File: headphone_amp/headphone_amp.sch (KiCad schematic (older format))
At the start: 16 parts, among them J1 Molex_SL_01x03_Male, J2 Molex_SL_01x02_Male

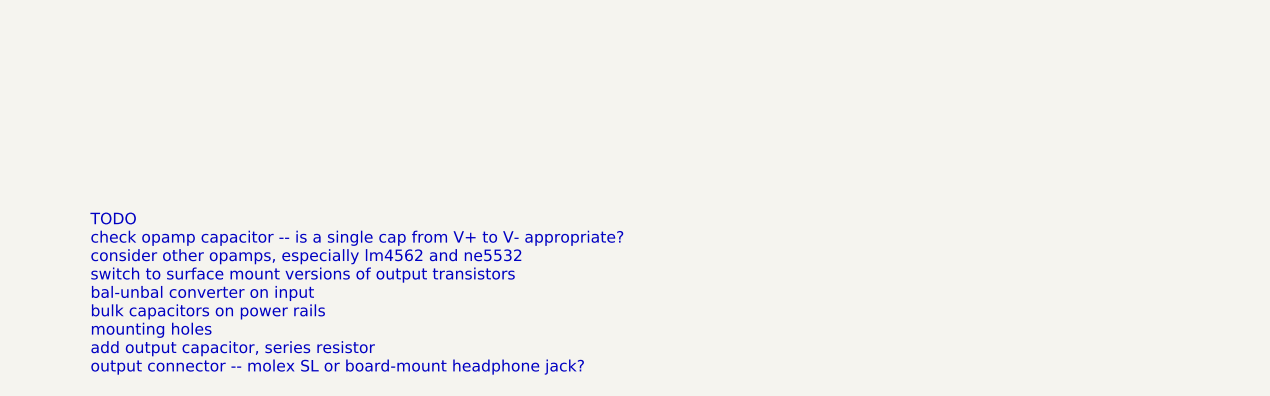
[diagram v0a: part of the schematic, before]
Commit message: update TODO and add license comment
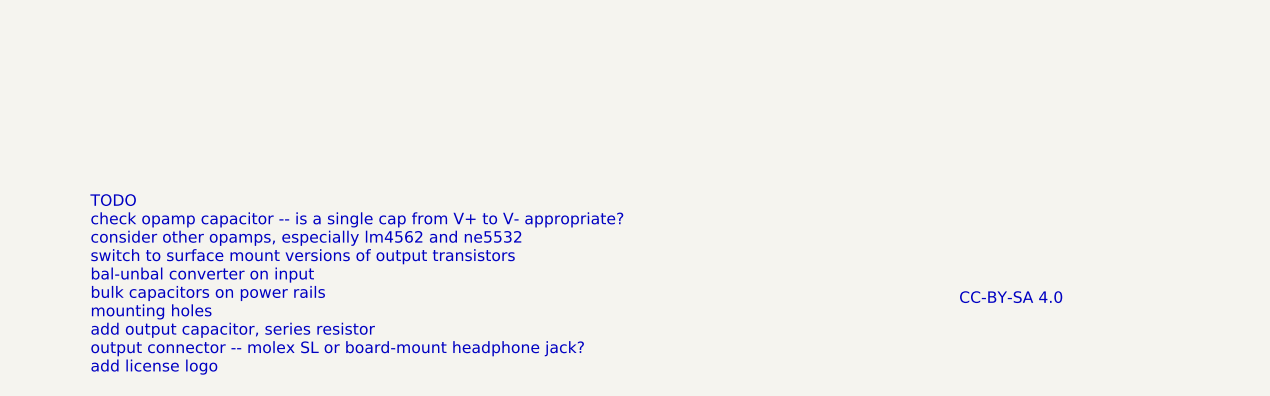
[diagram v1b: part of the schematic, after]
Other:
- note added: "CC-BY-SA 4.0"
- note added: "TODO\ncheck opamp capacitor -- is a single cap from V+ to V- appropriate?\nconsider other opamps, especially lm4562 and ne5532\nswitch to surface mount versions of output transistors\nbal-unbal converter on input\nbulk capacitors on power rails\nmounting holes\nadd output capacitor, series resistor\noutput connector -- molex SL or board-mount headphone jack?\nadd license logo"
- note removed: "TODO\ncheck opamp capacitor -- is a single cap from V+ to V- appropriate?\nconsider other opamps, especially lm4562 and ne5532\nswitch to surface mount versions of output transistors\nbal-unbal converter on input\nbulk capacitors on power rails\nmounting holes\nadd output capacitor, series resistor\noutput connector -- molex SL or board-mount headphone jack?"
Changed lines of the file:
@@
 Connection ~ 2150 1150
 Text Notes 1300 7550 0    50   ~ 0
-TODO\ncheck opamp capacitor -- is a single cap from V+ to V- appropriate?\nconsider other opamps, especially lm4562 and ne5532\nswitch to surface mount versions of output transistors\nbal-unbal converter on input\nbulk capacitors on power rails\nmounting holes\nadd output capacitor, series resistor\noutput connector -- molex SL or board-mount headphone jack?
+TODO\ncheck opamp capacitor -- is a single cap from V+ to V- appropriate?\nconsider other opamps, especially lm4562 and ne5532\nswitch to surface mount versions of output transistors\nbal-unbal converter on input\nbulk capacitors on power rails\nmounting holes\nadd output capacitor, series resistor\noutput connector -- molex SL or board-mount headphone jack?\nadd license logo
 $Comp
 L Connector_gkeeth:Molex_SL_01x02_Male J2
@@
 Text Label 2450 3150 0    50   ~ 0
 cold
+Text Notes 5100 7250 0    50   ~ 0
+CC-BY-SA 4.0
 $EndSCHEMATC

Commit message: Complete initial schematic for headphone amplifier
Features present:
- left and right channels
- input connectors, output jack
- balanced-to-unbalanced converters
- power connector
- bulk capacitance
- mounting holes

Remaining TODO:
- relay
- footprints
- surface mount output transistors
- output jack grounding?
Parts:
- removed R?: 10k, symbol Device:R
- removed U? (x3): TL072, symbol Amplifier_Operational:TL072
- added C1, C2, C4, C5: 22p, symbol Device:C
- added C3, C6, C8, C9: 220u, symbol Device:CP1
- added D3, D4: 1N4148WS, Diode_SMD:D_SOD-323, symbol Diode:1N4148WS
- added H1, H2: MountingHole_Pad, MountingHole:MountingHole_4.5mm_Pad, symbol Mechanical:MountingHole_Pad
- added J2: Molex_SL_01x02_Male, Connector_Molex_SL:Molex_SL_A-70543-0001_1x02_P2.54mm_Vertical, symbol Connector_gkeeth:Molex_SL_01x02_Male
- added J4: AudioJack3, symbol Connector:AudioJack3
- added Q3: MPSA42, Package_TO_SOT_THT:TO-92_Inline, symbol Transistor_BJT:MPSA42
- added Q4: MPSA92, Package_TO_SOT_THT:TO-92_Inline, symbol Transistor_BJT:MPSA92
- added R10, R12, R4: 22k, symbol Device:R
- added R11, R3, R9: 10k, symbol Device:R
- added R13: 4.7k, symbol Device:R
- added R14, R15: 10, symbol Device:R
- added R16, R8: 47, symbol Device:R
- added U1: NE5532, symbol Amplifier_Operational:NE5532
- gave numbers to parts that had none: 10
- renumbered J2 to J1, J1 to J3
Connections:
- net labels added: left_cold, left_hot, right_cold, right_hot
- net labels removed: cold, hot
- wire segments 53 -> 125
- no-connect marks 1 -> 0
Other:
- note added: "TODO\nconsider other opamps, especially lm4562 and TL072\nswitch to surface mount versions of output transistors\noutput connector -- molex SL or board-mount headphone jack?\nhow to ground headphone jack?\noutput relay"
- note added: "fc = 1/(2 x pi x 22k x 22p) = 330kHz\nBandwidth limiting capacitors may be unnecessary"
- note removed: "TODO\ncheck opamp capacitor -- is a single cap from V+ to V- appropriate?\nconsider other opamps, especially lm4562 and ne5532\nswitch to surface mount versions of output transistors\nbal-unbal converter on input\nbulk capacitors on power rails\nmounting holes\nadd output capacitor, series resistor\noutput connector -- molex SL or board-mount headphone jack?\nadd license logo"
- moved on the sheet: C7, D1, D2, J1, J3, Q1, Q2, R1, R2, R5, R6, R7

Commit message: change output connector to molex connector (wired to panel mount jack)
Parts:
- removed J4: AudioJack3, symbol Connector:AudioJack3
- added J3: Molex_SL_01x03_Male, Connector_Molex_SL:Molex_SL_A-70543-0002_1x03_P2.54mm_Vertical, symbol Connector_gkeeth:Molex_SL_01x03_Male
- renumbered J3 to J4
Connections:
- net labels added: gnd_out, left_out, right_out
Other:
- note added: "Connect output connector ground to star ground"
- note added: "TODO\nconsider other opamps, especially lm4562 and TL072\nswitch to surface mount versions of output transistors\nheadphone jack ground to chassis...?"
- note removed: "TODO\nconsider other opamps, especially lm4562 and TL072\nswitch to surface mount versions of output transistors\noutput connector -- molex SL or board-mount headphone jack?\nhow to ground headphone jack?\noutput relay"
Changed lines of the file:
@@
 	7650 1000 7650 1050
 $Comp
-L Connector_gkeeth:Molex_SL_01x03_Male J3
+L Connector_gkeeth:Molex_SL_01x03_Male J4
 U 1 1 5D79F9DA
 P 850 7100
-F 0 "J3" H 958 7381 50  0000 C CNN
+F 0 "J4" H 958 7381 50  0000 C CNN
 F 1 "Molex_SL_01x03_Male" H 958 7290 50  0000 C CNN
 F 2 "Connector_Molex_SL:Molex_SL_A-70543-0002_1x03_P2.54mm_Vertical" H 850 7100 50  0001 C CNN
@@
 Connection ~ 1500 7550
 Text Notes 7750 5400 0    50   ~ 0
-TODO\nconsider other opamps, especially lm4562 and TL072\nswitch to surface mount versions of output transistors\noutput connector -- molex SL or board-mount headphone jack?\nhow to ground headphone jack?\noutput relay
+TODO\nconsider other opamps, especially lm4562 and TL072\nswitch to surface mount versions of output transistors\nheadphone jack ground to chassis...?
 $Comp
 L Connector_gkeeth:Molex_SL_01x02_Male J1
@@
 Wire Wire Line
 	2400 2200 2750 2200
-$Comp
-L Connector:AudioJack3 J4
-U 1 1 5D7EE19B
-P 7550 6250
-F 0 "J4" H 7270 6183 50  0000 R CNN
-F 1 "AudioJack3" H 7270 6274 50  0000 R CNN
-F 2 "" H 7550 6250 50  0001 C CNN
-F 3 "~" H 7550 6250 50  0001 C CNN
-	1    7550 6250
-	-1   0    0    1
-$EndComp
 Wire Wire Line
 	4600 1800 4600 2100
@@
 	7000 2550 7000 6150
 Wire Wire Line
-	7000 6150 7350 6150
+	7000 6150 7850 6150
 Wire Wire Line
 	3450 5900 3450 6200
@@
 Connection ~ 5800 6250
 Wire Wire Line
-	6800 6250 7350 6250
+	6800 6250 7850 6250
 Wire Wire Line
 	5800 2550 5900 2550
@@
 	7150 6500 7150 6350
 Wire Wire Line
-	7150 6350 7350 6350
+	7150 6350 7850 6350
 $Comp
 L Mechanical:MountingHole_Pad H1
@@
 	1    0    0    -1
 $EndComp
+$Comp
+L Connector_gkeeth:Molex_SL_01x03_Male J3
+U 1 1 5D93DF57
+P 8050 6250
+F 0 "J3" H 8022 6274 50  0000 R CNN
+F 1 "Molex_SL_01x03_Male" H 8022 6183 50  0000 R CNN
+F 2 "Connector_Molex_SL:Molex_SL_A-70543-0002_1x03_P2.54mm_Vertical" H 8050 6250 50  0001 C CNN
+F 3 "https://www.molex.com/pdm_docs/sd/705430001_sd.pdf" H 8050 6250 50  0001 C CNN
+	1    8050 6250
+	-1   0    0    -1
+$EndComp
+Text Label 7300 6150 0    50   ~ 0
+left_out
+Text Label 7300 6250 0    50   ~ 0
+right_out
+Text Label 7300 6350 0    50   ~ 0
+gnd_out
+Text Notes 7500 6500 0    50   ~ 0
+Connect output connector ground to star ground
 $EndSCHEMATC

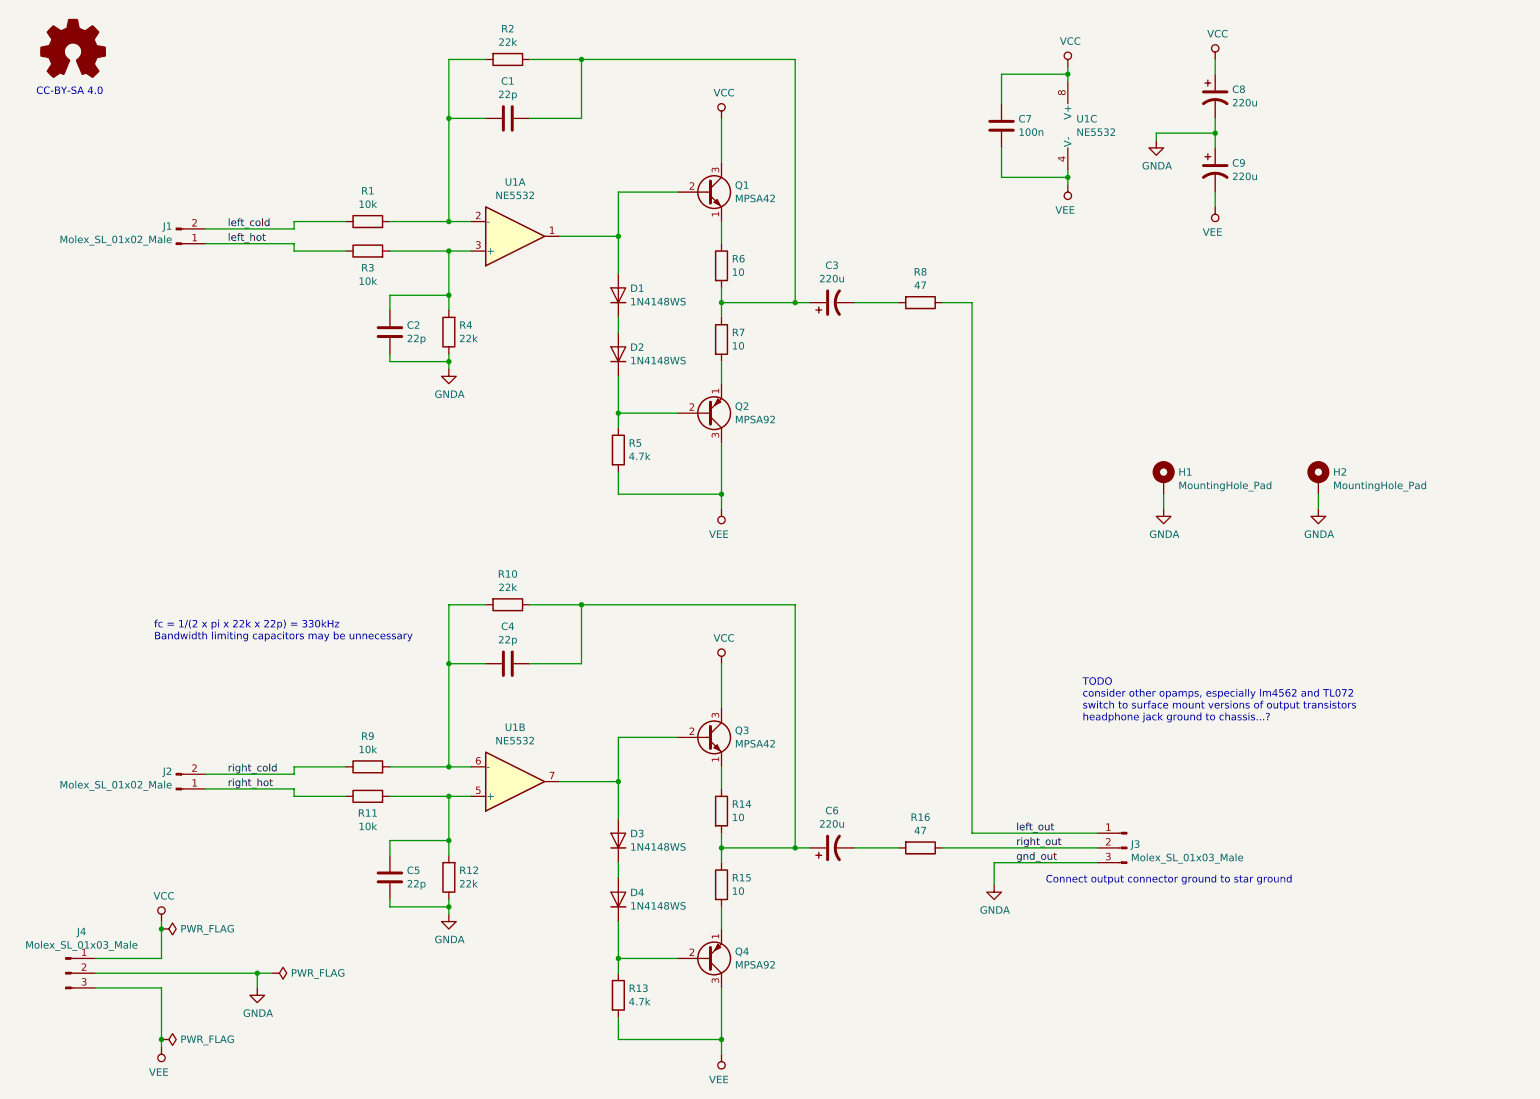
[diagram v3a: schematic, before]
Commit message: add all footprints
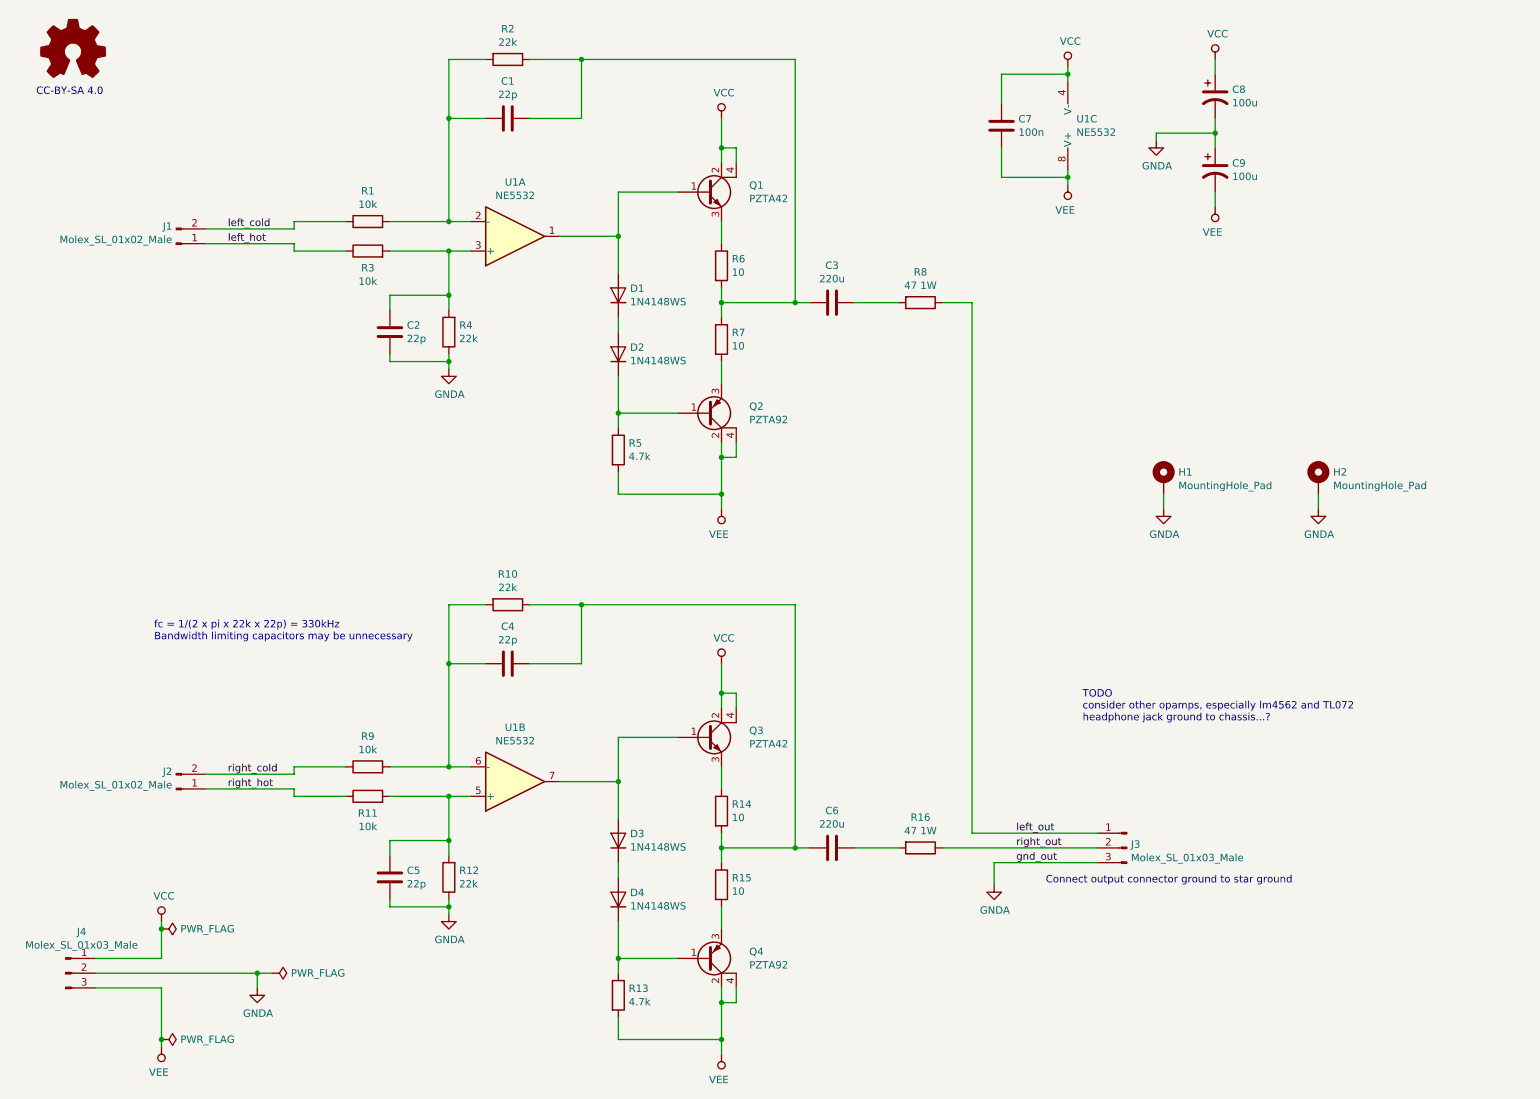
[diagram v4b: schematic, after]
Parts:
- removed C3, C6: 220u, symbol Device:CP1
- removed Q1, Q3: MPSA42, Package_TO_SOT_THT:TO-92_Inline, symbol Transistor_BJT:MPSA42
- removed Q2, Q4: MPSA92, Package_TO_SOT_THT:TO-92_Inline, symbol Transistor_BJT:MPSA92
- added C3, C6: 220u, Capacitor_THT:C_Radial_D12.5mm_H25.0mm_P5.00mm, symbol Device:C
- added Q1, Q3: PZTA42, Package_TO_SOT_SMD:SOT-223, symbol Device:Q_NPN_BCEC
- added Q2, Q4: PZTA92, Package_TO_SOT_SMD:SOT-223, symbol Device:Q_PNP_BCEC
- C1, C2, C4, C5: footprint (none) -> Capacitor_SMD:C_0603_1608Metric_Pad1.05x0.95mm_HandSolder
- C7: footprint (none) -> Capacitor_SMD:C_0805_2012Metric_Pad1.15x1.40mm_HandSolder; Dielectric (none) -> X7R; Distributor (none) -> Digikey; Distributor PN (none) -> 490-8051-1-ND; Manufacturer (none) -> Murata; Manufacturer PN (none) -> GCM21BR72A104KA37K; URL (none) -> https://www.digikey.com/product-detail/en/murata-electronic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; Unit Price (none) -> 0.43
- C8, C9: value 220u -> 100u; footprint (none) -> Capacitor_THT:CP_Radial_D6.3mm_P2.50mm; Dielectric (none) -> Electrolytic; Distributor (none) -> Digikey; Distributor PN (none) -> 493-1081-ND; Manufacturer (none) -> Nichicon; Manufacturer PN (none) -> UVR1V101MED; URL (none) -> https://www.digikey.com/product-detail/en/nichicon/UVR1V101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; Unit Price (none) -> 0.26; Voltage Rating (none) -> 35V
- R1, R10, R11, R12, R13, R2, R3, R4, R5, R9: footprint (none) -> Resistor_SMD:R_0603_1608Metric_Pad1.05x0.95mm_HandSolder
- R14, R15, R6, R7: footprint (none) -> Resistor_SMD:R_0603_1608Metric_Pad1.05x0.95mm_HandSolder; Distributor (none) -> Digikey; Distributor PN (none) -> RNCP0603FTD10R0CT-ND; Manufacturer (none) -> Stackpole; Manufacturer PN (none) -> RNCP0603FTD10R0; URL (none) -> https://www.digikey.com/product-detail/en/stackpole-electro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; Unit Price (none) -> 0.10
- R16, R8: value 47 -> 47 1W; footprint (none) -> Resistor_THT:R_Axial_DIN0414_L11.9mm_D4.5mm_P15.24mm_Horizontal; Distributor (none) -> Digikey; Distributor PN (none) -> BC4537CT-ND; Manufacturer (none) -> Vishay BC; Manufacturer PN (none) -> MBE04140C4709FC100; URL (none) -> https://www.digikey.com/product-detail/en/vishay-bc-compone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; Unit Price (none) -> 0.69
- U1: footprint (none) -> Package_SO:SOIC-8_3.9x4.9mm_P1.27mm; Distributor (none) -> Digikey; Distributor PN (none) -> NE5532AD8R2GOSCT-ND; Manufacturer (none) -> ON Semiconductor; Manufacturer PN (none) -> NE5532AD8R2G
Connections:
- net VCC: now also U1.4 (V-), Q1.2 (C), Q1.4 (C), Q3.2 (C), Q3.4 (C); no longer U1.8 (V+)
- net VEE: now also U1.8 (V+), Q2.2 (C), Q2.4 (C), Q4.2 (C), Q4.4 (C); no longer U1.4 (V-)
- net at R6.1: now also Q1.3 (E)
- net at C1.1, R2.1, R6.2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: now also C3.2
- net at R7.2: now also Q2.3 (E)
- net at D1.2 (A), U1.1: now also Q1.1 (B)
- net at D2.1 (K), R5.1: now also Q2.1 (B)
- net at R14.1: now also Q3.3 (E)
- net at C4.1, R10.1, R14.2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: now also C6.2
- net at R15.2: now also Q4.3 (E)
- net at D3.2 (A), U1.7: now also Q3.1 (B)
- net at D4.1 (K), R13.1: now also Q4.1 (B)
- net at R8.2: now also C3.1
- net at R16.2: now also C6.1
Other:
- note added: "TODO\nconsider other opamps, especially lm4562 and TL072\nheadphone jack ground to chassis...?"
- note removed: "TODO\nconsider other opamps, especially lm4562 and TL072\nswitch to surface mount versions of output transistors\nheadphone jack ground to chassis...?"

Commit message: change connectors to be horizontal, and add initial *rough* placement of parts to layout
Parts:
- J1, J2: footprint Connector_Molex_SL:Molex_SL_A-70543-0001_1x02_P2.54mm_Vertical -> Connector_Molex_SL:Molex_SL_A-70553-0001_1x02_P2.54mm_Horizontal
- J3, J4: footprint Connector_Molex_SL:Molex_SL_A-70543-0002_1x03_P2.54mm_Vertical -> Connector_Molex_SL:Molex_SL_A-70553-0002_1x03_P2.54mm_Horizontal
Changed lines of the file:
@@
 F 0 "J4" H 958 7381 50  0000 C CNN
 F 1 "Molex_SL_01x03_Male" H 958 7290 50  0000 C CNN
-F 2 "Connector_Molex_SL:Molex_SL_A-70543-0002_1x03_P2.54mm_Vertical" H 850 7100 50  0001 C CNN
+F 2 "Connector_Molex_SL:Molex_SL_A-70553-0002_1x03_P2.54mm_Horizontal" H 850 7100 50  0001 C CNN
 F 3 "https://www.molex.com/pdm_docs/sd/705430001_sd.pdf" H 850 7100 50  0001 C CNN
 	1    850  7100
@@
 F 0 "J1" H 1573 2032 50  0000 R CNN
 F 1 "Molex_SL_01x02_Male" H 1573 2123 50  0000 R CNN
-F 2 "Connector_Molex_SL:Molex_SL_A-70543-0001_1x02_P2.54mm_Vertical" H 1600 2150 50  0001 C CNN
+F 2 "Connector_Molex_SL:Molex_SL_A-70553-0001_1x02_P2.54mm_Horizontal" H 1600 2150 50  0001 C CNN
 F 3 "https://www.molex.com/pdm_docs/sd/705430001_sd.pdf" H 1600 2150 50  0001 C CNN
 	1    1600 2150
@@
 F 0 "J2" H 1573 5732 50  0000 R CNN
 F 1 "Molex_SL_01x02_Male" H 1573 5823 50  0000 R CNN
-F 2 "Connector_Molex_SL:Molex_SL_A-70543-0001_1x02_P2.54mm_Vertical" H 1600 5850 50  0001 C CNN
+F 2 "Connector_Molex_SL:Molex_SL_A-70553-0001_1x02_P2.54mm_Horizontal" H 1600 5850 50  0001 C CNN
 F 3 "https://www.molex.com/pdm_docs/sd/705430001_sd.pdf" H 1600 5850 50  0001 C CNN
 	1    1600 5850
@@
 F 0 "J3" H 8022 6274 50  0000 R CNN
 F 1 "Molex_SL_01x03_Male" H 8022 6183 50  0000 R CNN
-F 2 "Connector_Molex_SL:Molex_SL_A-70543-0002_1x03_P2.54mm_Vertical" H 8050 6250 50  0001 C CNN
+F 2 "Connector_Molex_SL:Molex_SL_A-70553-0002_1x03_P2.54mm_Horizontal" H 8050 6250 50  0001 C CNN
 F 3 "https://www.molex.com/pdm_docs/sd/705430001_sd.pdf" H 8050 6250 50  0001 C CNN
 	1    8050 6250
